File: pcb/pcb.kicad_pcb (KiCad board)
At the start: 4 copper layers, 170.2 x 137.2 mm, 173 parts, among them J1 Barrel_Jack, J10 Screw_Terminal_01x08, J11 Conn_01x08_Male, J12 Conn_01x08_Male, J13 Conn_01x08_Male, J14 Conn_01x08_Male, J15 Conn_01x02_Male, J2 Barrel_Jack, J3 Screw_Terminal_01x02, J4 Screw_Terminal_01x02, J5 Conn_02x05_Odd_Even, J6 Conn_01x06_Male, J7 Screw_Terminal_01x08, J8 Screw_Terminal_01x08, J9 Screw_Terminal_01x08, SW1 SW_SPDT, SW2 SW_SPDT, U1 CPC5001G, U10 LTV-847, U11 LTV-847, U12 MCP23017-E_SP, U13 MCP23017-E_SP, U2 MCP23017-E_SP, U3 LTV-847, U4 LTV-847, U5 LTV-847, U6 LTV-847, U7 MCP23017-E_SP, U8 LTV-847, U9 LTV-847

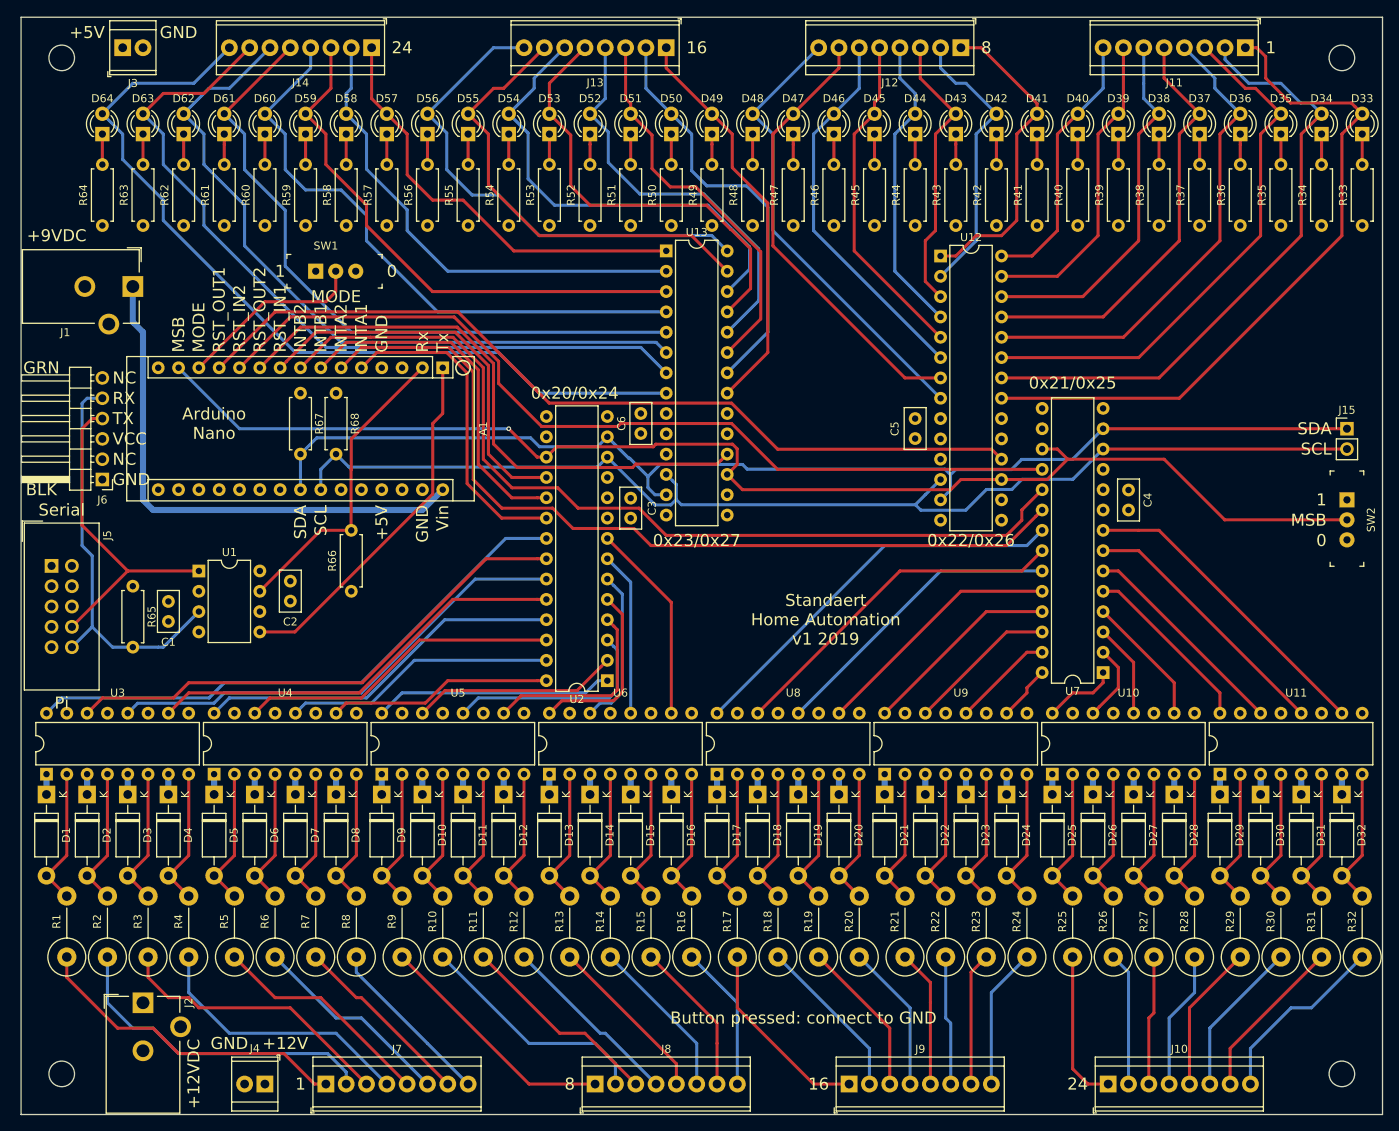
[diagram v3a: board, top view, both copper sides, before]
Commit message: Silkscreen, positioning, rounded corners
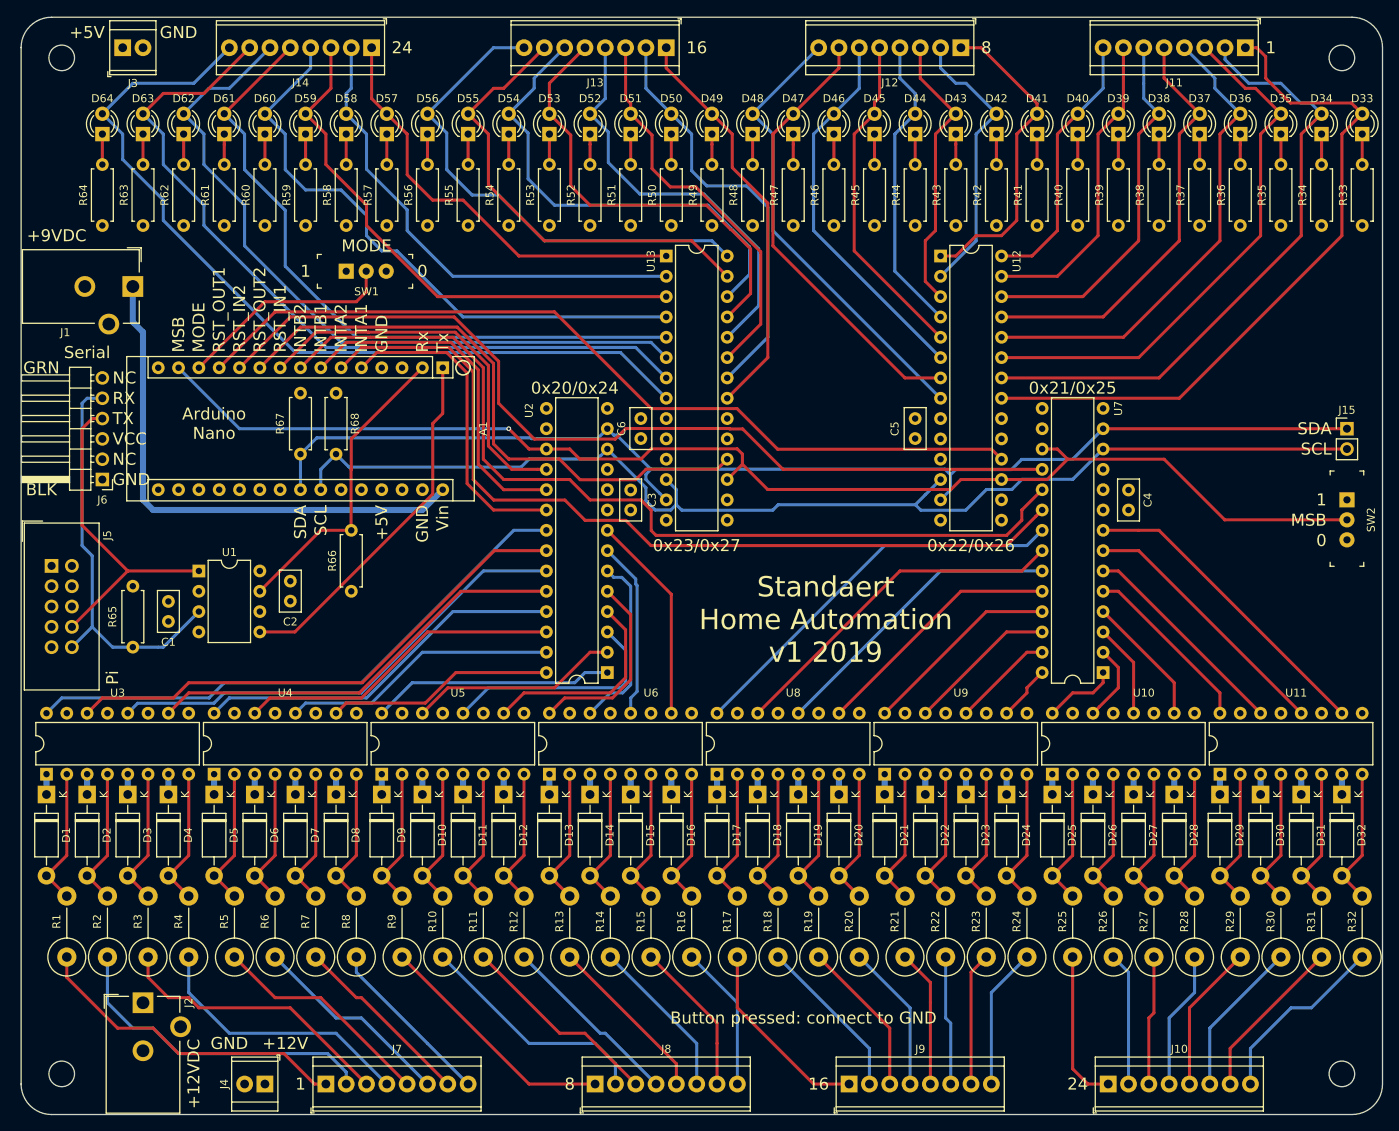
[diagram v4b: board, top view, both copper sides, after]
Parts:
- moved SW1 3.81 mm to (124.5, 52.1)
- moved C3 1.02 mm to (160.0, 81.9)
- moved U2 1.01 mm to (157.1, 102.2)
- moved C6 0.64 mm to (161.3, 70.5)
- moved U13 0.63 mm to (164.5, 50.2)
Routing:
- net /PRG_MODE: track 23.7 -> 27.5 mm
- net /Input 1/IN13: track 20.0 -> 22.6 mm
- net SCL: track 147.4 -> 149.7 mm
- net /~RESET_IN2: track 112.8 -> 115.0 mm
- net /Input 1/IN10: track 27.2 -> 29.2 mm
- net /Input 1/IN14: track 20.5 -> 22.2 mm
- net /Input 1/IN11: track 24.7 -> 26.3 mm
- net /Input 1/IN12: track 22.6 -> 24.2 mm
- net /INTB2: track 114.4 -> 115.8 mm
- net /~RESET_OUT2: track 74.4 -> 75.4 mm
- net /Input 1/IN15: track 25.2 -> 26.2 mm
- net /~RESET_IN1: track 49.1 -> 48.1 mm
- net /Output 2/Out2: track 48.7 -> 49.3 mm
- net /Output 2/Out1: track 52.0 -> 52.6 mm
- net /Output 2/Out5: track 58.2 -> 58.9 mm
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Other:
- outline, holes or cut-outs redrawn

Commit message: version that went into production
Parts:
- J15: value Conn_01x02_Male -> Conn_01x04_Male; footprint Connector_PinHeader_2.54mm:PinHeader_1x02_P2.54mm_Vertical -> Connector_PinHeader_2.54mm:PinHeader_1x04_P2.54mm_Vertical
- moved SW2 3.17 mm to (249.6, 83.8)
- moved J15 2.54 mm to (249.6, 69.2)
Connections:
- J15 pad 1: SDA -> +5V
- J15 pad 2: SCL -> SDA
- SW1 pad 1: Net-(SW1-Pad1) -> +5V
- SW1 pad 3: Net-(SW1-Pad3) -> GND
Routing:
- net /MSB: track 165.7 -> 167.0 mm
